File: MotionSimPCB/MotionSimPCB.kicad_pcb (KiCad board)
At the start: 2 copper layers, 56 x 70 mm, 44 parts, among them J1 Conn_01x02, J10 Conn_01x02, J11 Raspberry_Pi_4, J12 AudioJack2, J2 Conn_01x08_Pin, J3 Conn_01x03, J4 Conn_01x03, J5 Conn_01x03, J6 Conn_01x03, J7 Conn_01x02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

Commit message: cleanup silkscreen
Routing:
- net +3.3V: track 99.7 -> 108.1 mm
- net Net-(U1-REGOUT): track 0.21 -> 1.99 mm
- net Net-(U1-CPOUT): track 0.18 -> 1.84 mm
- net Net-(D2-A): track 0.00 -> 1.65 mm
- net /RC_PPM: track 84.7 -> 83.2 mm
- net GND: vias 43 -> 49
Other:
- board text added: "3.3V"
- board text added: "RCPPM"
- board text added: "SCL"
- board text added: "SDA"
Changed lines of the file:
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@@
 		(tags "QFN 0.5")
 		(property "Reference" "U1"
-			(at 0 -3.375 90)
+			(at -3.25 -1.5 180)
 			(layer "F.SilkS")
 			(effects
@@
 		(tags "3.5mm audio cui horizontal jack stereo")
 		(property "Reference" "J12"
-			(at 0 -9.9 90)
+			(at 3.95 7 180)
 			(layer "F.SilkS")
 			(effects
@@
 		)
 	)
+	(gr_text "RCPPM"
+		(at 137.25 53.75 0)
+		(layer "F.SilkS")
+		(effects
+			(font
+				(size 1 1)
+				(thickness 0.2)
+				(bold yes)
+			)
+			(justify left bottom)
+		)
+	)
 	(gr_text "GND"
 		(at 115.25 75 0)
@@
 	)
 	(gr_text "T14"
-		(at 126 100.5 90)
+		(at 124.25 100.25 0)
 		(layer "F.SilkS")
 		(effects
@@
 		)
 	)
+	(gr_text "GND"
+		(at 133 87 0)
+		(layer "F.SilkS")
+		(effects
+			(font
+				(size 1 1)
+				(thickness 0.1)
+			)
+			(justify left bottom)
+		)
+	)
 	(gr_text "+5V"
 		(at 112.5 84 0)
@@
 		)
 	)
+	(gr_text "3.3V"
+		(at 125.71 87.5 0)
+		(layer "F.SilkS")
+		(effects
+			(font
+				(size 0.75 0.75)
+				(thickness 0.1)
+			)
+			(justify left bottom)
+		)
+	)
 	(gr_text "DIR"
 		(at 135.75 100.5 0)
@@
 		)
 	)
+	(gr_text "GND"
+		(at 133.25 52.5 0)
+		(layer "F.SilkS")
+		(effects
+			(font
+				(size 1 1)
+				(thickness 0.1)
+			)
+			(justify left bottom)
+		)
+	)
 	(gr_text "STEP"
 		(at 130.5 100.5 0)
@@
 		)
 	)
+	(gr_text "5V"
+		(at 143.75 80 0)
+		(layer "F.SilkS")
+		(effects
+			(font
+				(size 0.75 0.75)
+				(thickness 0.1)
+			)
+			(justify left bottom)
+		)
+	)
 	(gr_text "STEP"
 		(at 141.5 100.625 0)
@@
 	)
 	(gr_text "PI 22"
-		(at 114.5 100.25 90)
+		(at 112.5 100.5 0)
 		(layer "F.SilkS")
 		(effects
@@
 		)
 	)
+	(gr_text "SDA"
+		(at 129.5 82 0)
+		(layer "F.SilkS")
+		(effects
+			(font
+				(size 1 1)
+				(thickness 0.1)
+			)
+			(justify left bottom)
+		)
+	)
+	(gr_text "SCL"
+		(at 137 82 0)
+		(layer "F.SilkS")
+		(effects
+			(font
+				(size 1 1)
+				(thickness 0.1)
+			)
+			(justify left bottom)
+		)
+	)
 	(gr_text "LED"
 		(at 107.75 82.5 90)
@@
 	)
 	(gr_text "T15"
-		(at 121 100.5 90)
+		(at 119.5 100.25 0)
 		(layer "F.SilkS")
 		(effects
@@
 	)
 	(via
+		(at 131 84)
+		(size 0.6)
+		(drill 0.3)
+		(layers "F.Cu" "B.Cu")
+		(free yes)
+		(net 2)
+	)
+	(via
 		(at 128.5 82)
 		(size 0.6)
@@
 	)
 	(via
+		(at 145 85)
+		(size 0.6)
+		(drill 0.3)
+		(layers "F.Cu" "B.Cu")
+		(free yes)
+		(net 2)
+	)
+	(via
 		(at 131.5 66)
 		(size 0.6)
@@
 	)
 	(via
+		(at 153 76)
+		(size 0.6)
+		(drill 0.3)
+		(layers "F.Cu" "B.Cu")
+		(free yes)
+		(net 2)
+	)
+	(via
 		(at 119 68.75)
 		(size 0.6)
@@
 	)
 	(via
+		(at 131 88)
+		(size 0.6)
+		(drill 0.3)
+		(layers "F.Cu" "B.Cu")
+		(free yes)
+		(net 2)
+	)
+	(via
 		(at 117.25 81.5)
 		(size 0.6)
@@
 	)
 	(via
+		(at 136 88)
+		(size 0.6)
+		(drill 0.3)
+		(layers "F.Cu" "B.Cu")
+		(free yes)
+		(net 2)
+	)
+	(via
 		(at 142 67.5)
 		(size 0.6)
@@
 	)
 	(via
+		(at 145 92)
+		(size 0.6)
+		(drill 0.3)
+		(layers "F.Cu" "B.Cu")
+		(free yes)
+		(net 2)
+	)
+	(via
 		(at 145.5 105.5)
 		(size 0.6)
@@
 	)
 	(segment
+		(start 124.75 84.1)
+		(end 124.75 85.75)
+		(width 0.2)
+		(layer "F.Cu")
+		(net 6)
+	)
+	(segment
 		(start 109.4375 51.75)
 		(end 109.4375 49.275)
@@
 	)
 	(segment
+		(start 122.379468 85)
+		(end 121.340968 86.0385)
+		(width 0.2)
+		(layer "F.Cu")
+		(net 18)
+	)
+	(segment
 		(start 112.5 94.25)
 		(end 117.25 94.25)
@@
 	)
 	(segment
+		(start 120 83.9125)
+		(end 122.25 81.6625)
+		(width 0.2)
+		(layer "F.Cu")
+		(net 18)
+	)
+	(segment
 		(start 116.526 43.474)
 		(end 121.749 43.474)
@@
 	)
 	(segment
+		(start 120.502362 86.0385)
+		(end 120 85.536138)
+		(width 0.2)
+		(layer "F.Cu")
+		(net 18)
+	)
+	(segment
 		(start 122.9 84.375)
 		(end 122.9 85)
@@
 	)
 	(segment
+		(start 121.340968 86.0385)
+		(end 120.502362 86.0385)
+		(width 0.2)
+		(layer "F.Cu")
+		(net 18)
+	)
+	(segment
 		(start 114.75 58.99)
 		(end 114.75 63.25)
@@
 	)
 	(segment
+		(start 120 85.536138)
+		(end 120 83.9125)
+		(width 0.2)
+		(layer "F.Cu")
+		(net 18)
+	)
+	(segment
 		(start 126.675 48.225)
 		(end 125.25 49.65)
@@
 	)
 	(segment
+		(start 122.9 85)
+		(end 122.379468 85)
+		(width 0.2)
+		(layer "F.Cu")
+		(net 18)
+	)
+	(segment
 		(start 122.525 44.25)
 		(end 124.925 44.25)
@@
 	)
 	(segment
+		(start 124.8 47.5)
+		(end 123.45 47.5)
+		(width 0.2)
+		(layer "F.Cu")
+		(net 35)
+	)
+	(segment
 		(start 125.25 47.95)
-		(end 125.1 47.8)
+		(end 124.8 47.5)
 		(width 0.2)
 		(layer "F.Cu")
@@
 	)
 	(segment
+		(start 118.275 47)
+		(end 119.55 47)
+		(width 0.2)
+		(layer "F.Cu")
+		(net 36)
+	)
+	(segment
+		(start 118 47.275)
+		(end 118.275 47)
+		(width 0.2)
+		(layer "F.Cu")
+		(net 36)
+	)
+	(segment
 		(start 118.375 47.4)
 		(end 118.25 47.275)
@@
 	)
 	(segment
-		(start 139.95 44.1)
-		(end 139.95 43.2)
+		(start 100.8 65.922107)
+		(end 100.401 65.523107)
 		(width 0.2)
 		(layer "F.Cu")
@@
 	)
 	(segment
-		(start 100.599 40.401)
-		(end 100.401 40.599)
+		(start 100.401 43.232411)
+		(end 103.232411 40.401)
 		(width 0.2)
 		(layer "F.Cu")
@@
 	)
 	(segment
-		(start 100.401 40.599)
-		(end 100.401 65.523107)
+		(start 103.232411 40.401)
+		(end 137.151 40.401)
 		(width 0.2)
 		(layer "F.Cu")
@@
 	(segment
 		(start 137.151 40.401)
-		(end 100.599 40.401)
+		(end 139.95 43.2)
 		(width 0.2)
 		(layer "F.Cu")
@@
 	)
 	(segment
-		(start 101.001 81.321)
-		(end 102.46 82.78)
+		(start 139.95 43.2)
+		(end 139.95 44.1)
 		(width 0.2)
 		(layer "F.Cu")
@@
 	)
 	(segment
-		(start 100.401 65.523107)
-		(end 100.8 65.922107)
+		(start 101.001 81.321)
+		(end 102.46 82.78)
 		(width 0.2)
 		(layer "F.Cu")
@@
 	)
 	(segment
-		(start 139.95 43.2)
-		(end 137.151 40.401)
+		(start 100.401 65.523107)
+		(end 100.401 43.232411)
 		(width 0.2)
 		(layer "F.Cu")

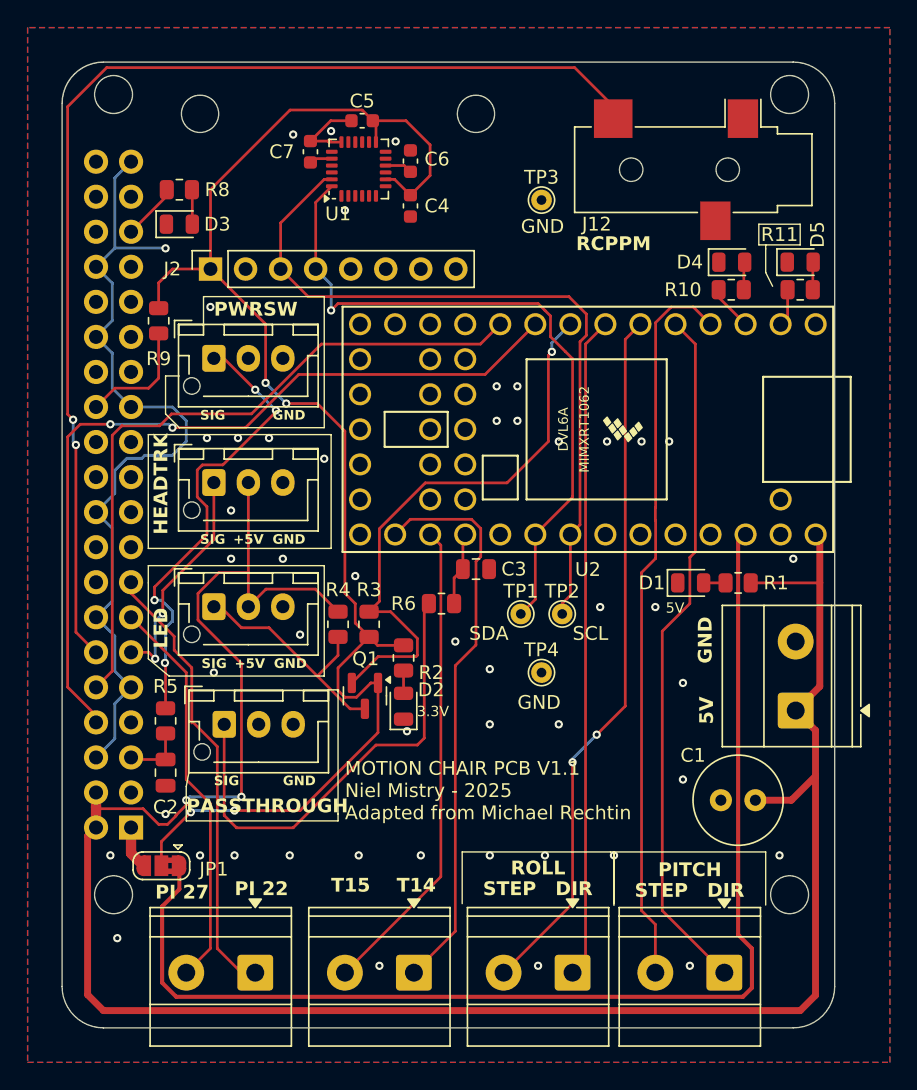
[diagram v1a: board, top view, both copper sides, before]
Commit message: fix drc, add protection
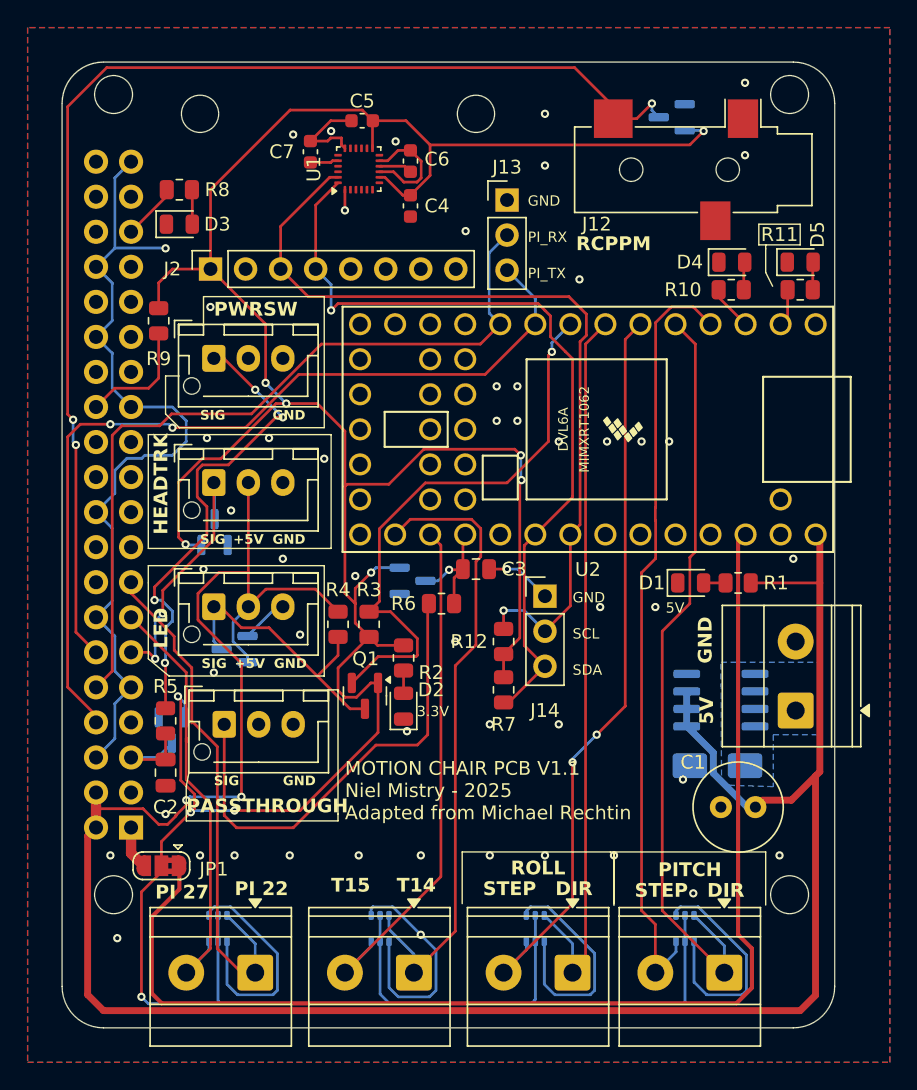
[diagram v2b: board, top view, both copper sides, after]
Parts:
- removed TP1, TP2, TP3, TP4: TestPoint, TestPoint:TestPoint_THTPad_D1.5mm_Drill0.7mm
- added D10: BAT54SDW, Package_TO_SOT_SMD:SOT-363_SC-70-6, B.Cu at (123.0, 102.8)
- added D11: BAT54S, Package_TO_SOT_SMD:SOT-23, B.Cu at (144.2, 44.0)
- added D12: BAT54S, Package_TO_SOT_SMD:SOT-23, B.Cu at (108.0, 88.4)
- added D13: BAT54S, Package_TO_SOT_SMD:SOT-23, B.Cu at (125.4, 77.6)
- added D14: BAT54S, Package_TO_SOT_SMD:SOT-23, B.Cu at (111.0, 74.1)
- added D15: BAT54S, Package_TO_SOT_SMD:SOT-23, B.Cu at (112.5, 82.5)
- added D6: SMAJ5.0A, Diode_SMD:D_SMA, B.Cu at (147.5, 91.0)
- added D7: BAT54SDW, Package_TO_SOT_SMD:SOT-363_SC-70-6, B.Cu at (134.3, 102.8)
- added D8: BAT54SDW, Package_TO_SOT_SMD:SOT-363_SC-70-6, B.Cu at (145.2, 102.8)
- added D9: BAT54SDW, Package_TO_SOT_SMD:SOT-363_SC-70-6, B.Cu at (111.3, 102.8)
- added J13: Conn_01x03, Connector_PinHeader_2.54mm:PinHeader_1x03_P2.54mm_Vertical, F.Cu at (132.2, 50.0)
- added J14: Conn_01x03, Connector_PinHeader_2.54mm:PinHeader_1x03_P2.54mm_Vertical, F.Cu at (135.0, 78.7)
- added Q2: IRF7404, Package_SO:SOIC-8_3.9x4.9mm_P1.27mm, B.Cu at (147.8, 86.2)
- added R12: 4.7k, Resistor_SMD:R_0805_2012Metric, F.Cu at (132.0, 82.0)
- added R7: 4.7k, Resistor_SMD:R_0805_2012Metric, F.Cu at (132.0, 85.5)
- R1: value 10k -> 2.2k
- R10, R11, R2, R8: value 10k -> 1k
- U1: footprint Sensor_Motion:InvenSense_QFN-24_4x4mm_P0.5mm -> Sensor_Motion:InvenSense_QFN-24_3x3mm_P0.4mm
- moved C1 0.50 mm to (150.2, 94.0)
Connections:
- J1 pad 1: +5V -> Net-(D6-A1)
- U1 pad 9: unconnected-(U1-AD0-Pad9) -> GND
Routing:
- net +3.3V: track 108.1 -> 268.8 mm, vias 4 -> 11
- net GND: track 67.9 -> 153.5 mm, vias 49 -> 52
- net +5V: track 162.7 -> 177.4 mm
- net SDA: track 50.2 -> 59.1 mm
- net SCL: track 53.8 -> 61.4 mm, vias 0 -> 1
- net /Controllers/PI_RX: track 50.2 -> 57.5 mm
- net /Controllers/PI_TX: track 59.0 -> 64.1 mm
- net /PITCH_DIR: track 50.5 -> 55.5 mm
- net /ROLL_DIR: track 48.0 -> 53.0 mm
- net /PI_P22: track 32.8 -> 37.8 mm
- net /T_P14: track 41.1 -> 46.0 mm
- net /RC_PPM: track 83.2 -> 87.6 mm, vias 2 -> 3
- net /PWR_OFF_SW: track 4.45 -> 7.82 mm
- net /LED_5V: track 17.7 -> 21.0 mm
- net /T_P15: track 35.0 -> 38.1 mm
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- added copper zone on B.Cu, net Net-(D6-A1)
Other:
- board text added: "PI_RX"
- board text added: "PI_TX"

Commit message: fix some issues
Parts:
- added C8: 0.1u, Capacitor_SMD:C_0603_1608Metric, B.Cu at (142.4, 80.8)
- added D16: BZV55C12, Diode_SMD:D_MiniMELF, B.Cu at (142.8, 86.3)
- added JP2: SolderJumper_2_Open, Jumper:SolderJumper-2_P1.3mm_Open_TrianglePad1.0x1.5mm, F.Cu at (153.8, 91.7)
- added R13: 100, Capacitor_SMD:C_0603_1608Metric, B.Cu at (145.6, 82.4)
- added R14: 100k, Capacitor_SMD:C_0603_1608Metric, B.Cu at (142.4, 82.4)
- added TP1: TestPoint_Flag, TestPoint:TestPoint_Pad_D2.0mm, F.Cu at (152.4, 77.4)
- moved D13 18.1 mm to (113.2, 91.0), turned to 180 degrees
- moved C3 2.71 mm to (127.6, 78.0), turned to 180 degrees
- moved R6 0.76 mm to (127.6, 80.0)
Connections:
- J3 pad 1: Net-(J3-Pin_1) -> /PWR_OFF_SW
- J4 pad 1: Net-(J4-Pin_1) -> /PASSTHRU
- Q2 pad 4: GND -> Net-(D16-A)
- R5 pad 1: Net-(J3-Pin_1) -> +3.3V
- R6 pad 1: Net-(J4-Pin_1) -> +3.3V
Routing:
- net /PASSTHRU: track 8.41 -> 66.0 mm, vias 1 -> 0
- net /PWR_OFF_SW: track 7.82 -> 45.3 mm, vias 0 -> 4
- net Net-(J3-Pin_1): track 34.8 -> 0.00 mm, vias 4 -> 0
- net Net-(J4-Pin_1): track 34.1 -> 0.00 mm
- net Net-(D16-A): track 0.00 -> 10.3 mm
- net +3.3V: track 268.8 -> 278.0 mm, vias 11 -> 10
- net GND: track 153.5 -> 160.1 mm, vias 52 -> 55
- net Net-(D6-A1): track 0.00 -> 4.21 mm
- net /HEAD_TRK: track 19.2 -> 18.6 mm
- added copper zone on B.Cu, net +5V

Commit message: fix clearance
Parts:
- added R15: 100, Capacitor_SMD:C_0603_1608Metric, F.Cu at (143.5, 94.7)
- added R16: 100, Capacitor_SMD:C_0603_1608Metric, F.Cu at (142.0, 94.7)
- added R17: 100, Capacitor_SMD:C_0603_1608Metric, F.Cu at (138.4, 94.7)
- added R18: 100, Capacitor_SMD:C_0603_1608Metric, F.Cu at (136.9, 94.7)
- added R19: 100, Capacitor_SMD:C_0603_1608Metric, F.Cu at (110.6, 100.0)
- added R20: 100, Capacitor_SMD:C_0603_1608Metric, F.Cu at (110.4, 96.6)
- added R21: 100, Capacitor_SMD:C_0603_1608Metric, F.Cu at (128.8, 94.7)
- added R22: 100, Capacitor_SMD:C_0603_1608Metric, F.Cu at (126.8, 94.7)
- added R24: 100, Capacitor_SMD:C_0603_1608Metric, F.Cu at (135.2, 41.4)
- added R25: 100, Capacitor_SMD:C_0603_1608Metric, F.Cu at (108.0, 75.8)
- Q2: value IRF7404 -> DMP2040USS
- U1: footprint Sensor_Motion:InvenSense_QFN-24_3x3mm_P0.4mm -> Sensor_Motion:InvenSense_QFN-24_4x4mm_P0.5mm
- moved C4 0.62 mm to (125.2, 49.8)
- moved C6 0.47 mm to (125.2, 46.7)
- moved C7 0.45 mm to (118.2, 46.1)
- moved JP1 0.27 mm to (107.3, 98.0)
- moved U1 0.18 mm to (121.7, 47.6)
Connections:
- D10 pad 3: /T_P14 -> /T_P14_C
- D10 pad 6: /T_P15 -> /T_P15_C
- D11 pad 3: /RC_PPM -> /RC_PPM_C
- D14 pad 3: /HEAD_TRK -> /HEAD_TRK_C
- D7 pad 3: /ROLL_DIR -> /ROLL_DIR_C
- D7 pad 6: /ROLL_STEP -> /ROLL_STEP_C
- D8 pad 3: /PITCH_DIR -> /PITCH_DIR_C
- D8 pad 6: /PITCH_STEP -> /PITCH_STEP_C
- D9 pad 3: /PI_P22 -> /PI_P22_C
- D9 pad 6: /PI_P27 -> /PI_P27_C
- J10 pad 1: /T_P14 -> /T_P14_C
- J10 pad 2: /T_P15 -> /T_P15_C
- J12 pad T: /RC_PPM -> /RC_PPM_C
- J5 pad 1: /HEAD_TRK -> /HEAD_TRK_C
- J7 pad 1: /PITCH_DIR -> /PITCH_DIR_C
- J7 pad 2: /PITCH_STEP -> /PITCH_STEP_C
- J8 pad 1: /ROLL_DIR -> /ROLL_DIR_C
- J8 pad 2: /ROLL_STEP -> /ROLL_STEP_C
- J9 pad 1: /PI_P22 -> /PI_P22_C
- J9 pad 2: /PI_P27 -> /PI_P27_C
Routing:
- net /PI_P22_C: track 0.00 -> 20.3 mm
- net /PITCH_DIR: track 55.5 -> 36.5 mm
- net /T_P14: track 46.0 -> 27.9 mm
- net /T_P15: track 38.1 -> 20.4 mm
- net /PITCH_DIR_C: track 0.00 -> 17.4 mm
- net /ROLL_DIR: track 53.0 -> 35.7 mm
- net /T_P15_C: track 0.00 -> 16.8 mm
- net /ROLL_STEP: track 54.0 -> 37.2 mm
- net /T_P14_C: track 0.00 -> 16.7 mm
- net /ROLL_DIR_C: track 0.00 -> 16.1 mm
- net /PITCH_STEP: track 56.0 -> 40.4 mm
- net /ROLL_STEP_C: track 0.00 -> 15.5 mm
- net /PITCH_STEP_C: track 0.00 -> 13.9 mm
- net /PI_P27: track 31.8 -> 17.9 mm
- net /PI_P22: track 37.6 -> 25.2 mm
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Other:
- board text added: "P27"
- board text removed: "PI 27"

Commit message: DNP D6
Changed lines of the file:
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@@
 		(tags "QFN 0.5")
 		(property "Reference" "U1"
-			(at 0 -3.375 90)
+			(at -3.35 0 180)
 			(layer "F.SilkS")
 			(effects
@@
 	)
 	(via
-		(at 120.5 50.75)
+		(at 120 50.8)
 		(size 0.6)
 		(drill 0.3)
@@
 		(width 0.2)
 		(layer "F.Cu")
-		(net 33)
-	)
-	(segment
-		(start 118.375 47.4)
-		(end 118.25 47.275)
-		(width 0.2)
-		(layer "F.Cu")
